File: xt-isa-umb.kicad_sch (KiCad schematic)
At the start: 15 parts, among them J1 Bus_ISA_8bit, U1 74LS138, U2 74LS08, U3 AS6C1008, U4 74HCT245

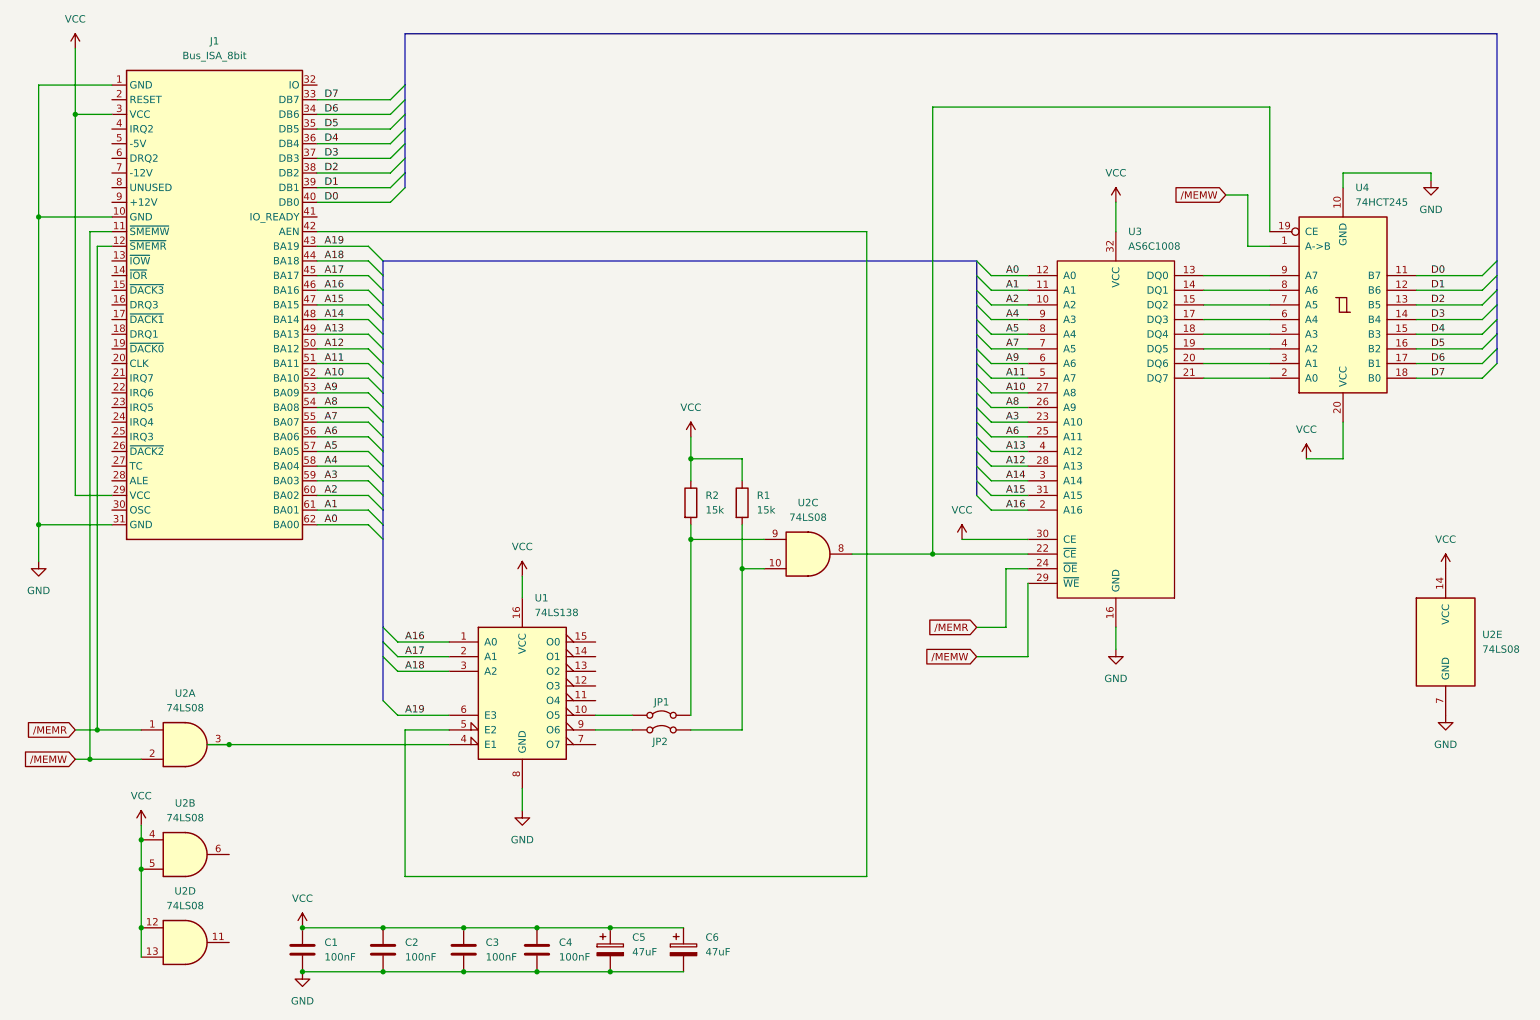
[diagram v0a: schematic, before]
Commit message: Add GND fill zone.
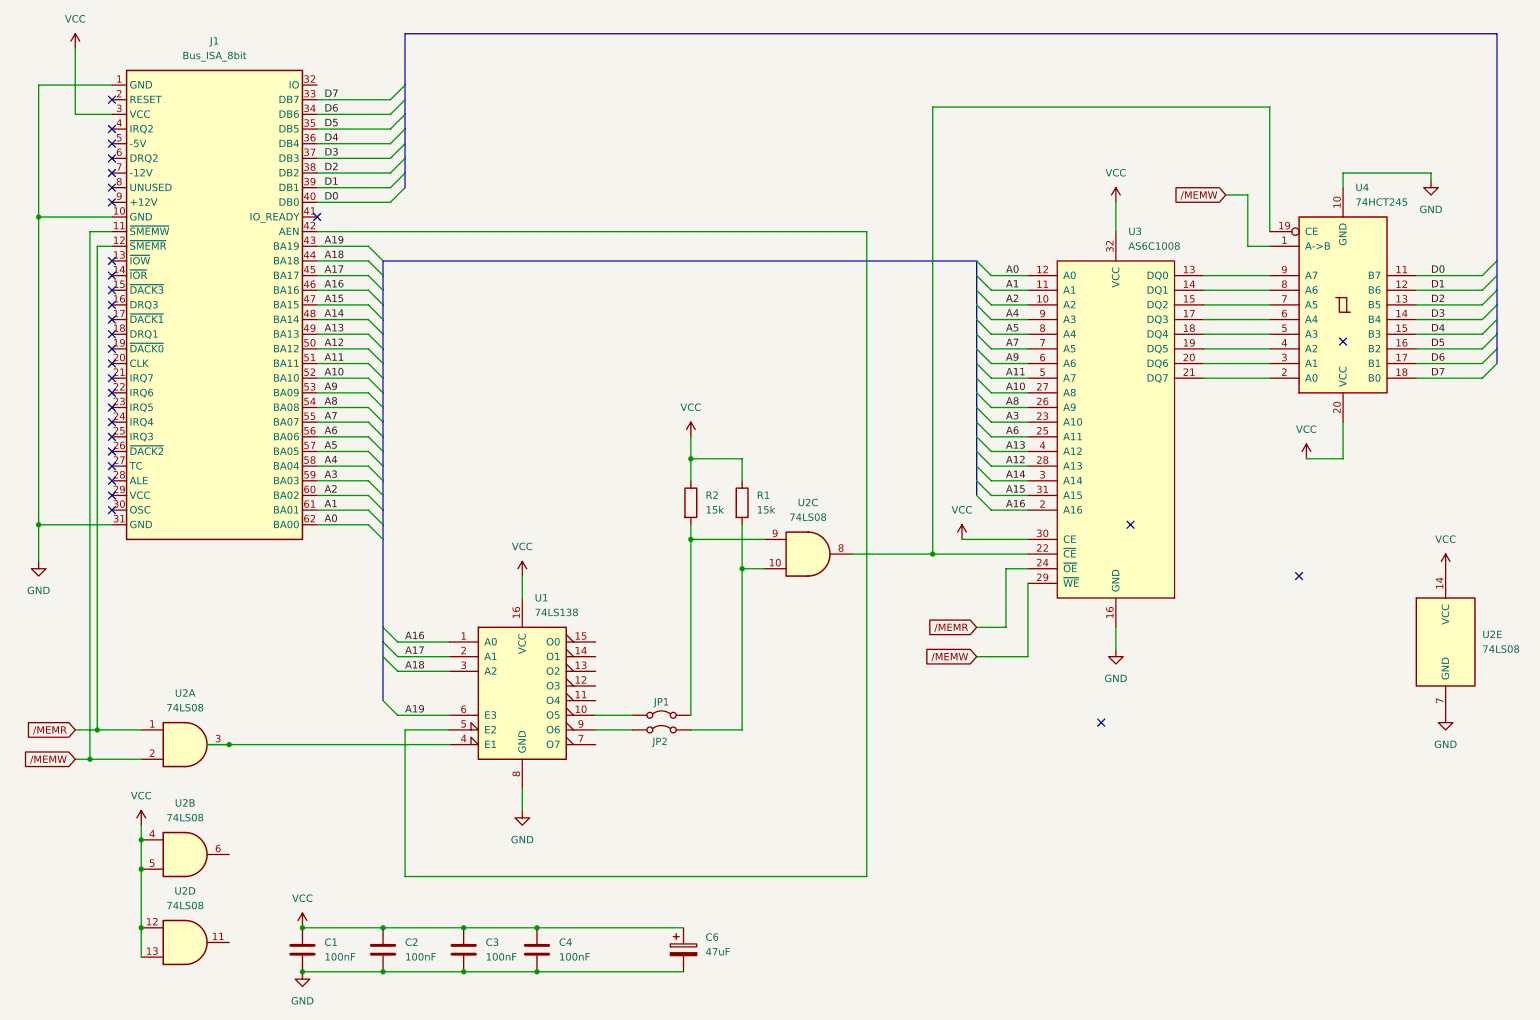
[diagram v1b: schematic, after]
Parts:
- removed C5: 47uF, Capacitor_THT:CP_Radial_D4.0mm_P2.00mm, symbol Device:C_Polarized
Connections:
- net VCC: no longer J1.29 (VCC)
- no-connect marks 0 -> 30
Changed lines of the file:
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@@
 	)
 	(junction
-		(at 119.38 176.53)
-		(diameter 0)
-		(color 0 0 0 0)
-	)
-	(junction
 		(at 66.04 176.53)
 		(diameter 0)
@@
 	)
 	(junction
-		(at 119.38 184.15)
-		(diameter 0)
-		(color 0 0 0 0)
-	)
-	(junction
 		(at 20.32 106.68)
 		(diameter 0)
@@
 	)
 	(junction
-		(at 26.67 35.56)
-		(diameter 0)
-		(color 0 0 0 0)
-	)
-	(junction
 		(at 133.35 109.22)
 		(diameter 0)
@@
 		(color 0 0 0 0)
 	)
+	(no_connect
+		(at 33.02 78.74)
+	)
+	(no_connect
+		(at 33.02 38.1)
+	)
+	(no_connect
+		(at 33.02 71.12)
+	)
+	(no_connect
+		(at 33.02 60.96)
+	)
+	(no_connect
+		(at 68.58 53.34)
+	)
+	(no_connect
+		(at 33.02 50.8)
+	)
+	(no_connect
+		(at 33.02 81.28)
+	)
+	(no_connect
+		(at 33.02 40.64)
+	)
+	(no_connect
+		(at 33.02 68.58)
+	)
+	(no_connect
+		(at 33.02 93.98)
+	)
+	(no_connect
+		(at 33.02 96.52)
+	)
+	(no_connect
+		(at 33.02 48.26)
+	)
+	(no_connect
+		(at 238.76 115.57)
+	)
+	(no_connect
+		(at 33.02 73.66)
+	)
+	(no_connect
+		(at 33.02 101.6)
+	)
+	(no_connect
+		(at 33.02 63.5)
+	)
+	(no_connect
+		(at 209.55 106.68)
+	)
+	(no_connect
+		(at 33.02 99.06)
+	)
+	(no_connect
+		(at 33.02 45.72)
+	)
+	(no_connect
+		(at 33.02 88.9)
+	)
+	(no_connect
+		(at 33.02 104.14)
+	)
+	(no_connect
+		(at 33.02 33.02)
+	)
+	(no_connect
+		(at 33.02 66.04)
+	)
+	(no_connect
+		(at 33.02 86.36)
+	)
+	(no_connect
+		(at 33.02 76.2)
+	)
+	(no_connect
+		(at 246.38 74.93)
+	)
+	(no_connect
+		(at 33.02 43.18)
+	)
+	(no_connect
+		(at 33.02 91.44)
+	)
+	(no_connect
+		(at 204.47 140.97)
+	)
+	(no_connect
+		(at 33.02 83.82)
+	)
 	(bus_entry
 		(at 77.47 73.66)
@@
 	(wire
 		(pts
-			(xy 33.02 101.6) (xy 26.67 101.6)
-		)
-		(stroke
-			(width 0)
-			(type default)
-		)
-	)
-	(wire
-		(pts
 			(xy 93.98 184.15) (xy 106.68 184.15)
 		)
@@
 		)
 	)
-	(wire
-		(pts
-			(xy 119.38 184.15) (xy 132.08 184.15)
-		)
-		(stroke
-			(width 0)
-			(type default)
-		)
-	)
 	(bus
 		(pts
@@
 	(wire
 		(pts
-			(xy 26.67 101.6) (xy 26.67 35.56)
-		)
-		(stroke
-			(width 0)
-			(type default)
-		)
-	)
-	(wire
-		(pts
 			(xy 191.77 129.54) (xy 191.77 116.84)
 		)
@@
 	(wire
 		(pts
-			(xy 106.68 176.53) (xy 119.38 176.53)
+			(xy 106.68 176.53) (xy 132.08 176.53)
 		)
 		(stroke
@@
 	(wire
 		(pts
-			(xy 119.38 176.53) (xy 132.08 176.53)
-		)
-		(stroke
-			(width 0)
-			(type default)
-		)
-	)
-	(wire
-		(pts
 			(xy 26.67 147.32) (xy 29.21 147.32)
 		)
@@
 	(wire
 		(pts
-			(xy 106.68 184.15) (xy 119.38 184.15)
+			(xy 106.68 184.15) (xy 132.08 184.15)
 		)
 		(stroke
@@
 					(unit 1)
 				)
-			)
-		)
-	)
-	(symbol
-		(lib_id "Device:C_Polarized")
-		(at 119.38 180.34 0)
-		(unit 1)
-		(exclude_from_sim no)
-		(in_bom yes)
-		(on_board yes)
-		(dnp no)
-		(fields_autoplaced yes)
-		(property "Reference" "C5"
-			(at 123.19 178.1809 0)
-			(effects
-				(font
-					(size 1.27 1.27)
-				)
-				(justify left)
-			)
-		)
-		(property "Value" "47uF"
-			(at 123.19 180.7209 0)
-			(effects
-				(font
-					(size 1.27 1.27)
-				)
-				(justify left)
-			)
-		)
-		(property "Footprint" "Capacitor_THT:CP_Radial_D4.0mm_P2.00mm"
-			(at 120.3452 184.15 0)
-			(effects
-				(font
-					(size 1.27 1.27)
-				)
-				(hide yes)
-			)
-		)
-		(property "Datasheet" "~"
-			(at 119.38 180.34 0)
-			(effects
-				(font
-					(size 1.27 1.27)
-				)
-				(hide yes)
-			)
-		)
-		(property "Description" "Polarized capacitor"
-			(at 119.38 180.34 0)
-			(effects
-				(font
-					(size 1.27 1.27)
-				)
-				(hide yes)
-			)
-		)
-		(pin "2"
-		)
-		(pin "1"
-		)
-		(instances
-			(project ""
-				(path "/35dd1e90-3905-4322-931d-7234df9aca70"
-					(reference "C5")
-					(unit 1)
-				)

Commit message: Add gerber files
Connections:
- no-connect marks 30 -> 38
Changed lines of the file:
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@@
+	)
+	(no_connect
+		(at 116.84 144.78)
 	)
 	(no_connect
@@
 	(no_connect
 		(at 33.02 93.98)
+	)
+	(no_connect
+		(at 116.84 132.08)
+	)
+	(no_connect
+		(at 53.34 179.07)
+	)
+	(no_connect
+		(at 116.84 137.16)
 	)
 	(no_connect
@@
 	(no_connect
 		(at 33.02 63.5)
+	)
+	(no_connect
+		(at 116.84 129.54)
 	)
 	(no_connect
@@
 	)
 	(no_connect
+		(at 53.34 163.83)
+	)
+	(no_connect
 		(at 33.02 43.18)
 	)
@@
 	)
 	(no_connect
+		(at 116.84 134.62)
+	)
+	(no_connect
 		(at 33.02 83.82)
 	)
+	(no_connect
+		(at 116.84 127)
+	)
 	(bus_entry
